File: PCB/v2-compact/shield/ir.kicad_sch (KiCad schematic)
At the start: 0 parts

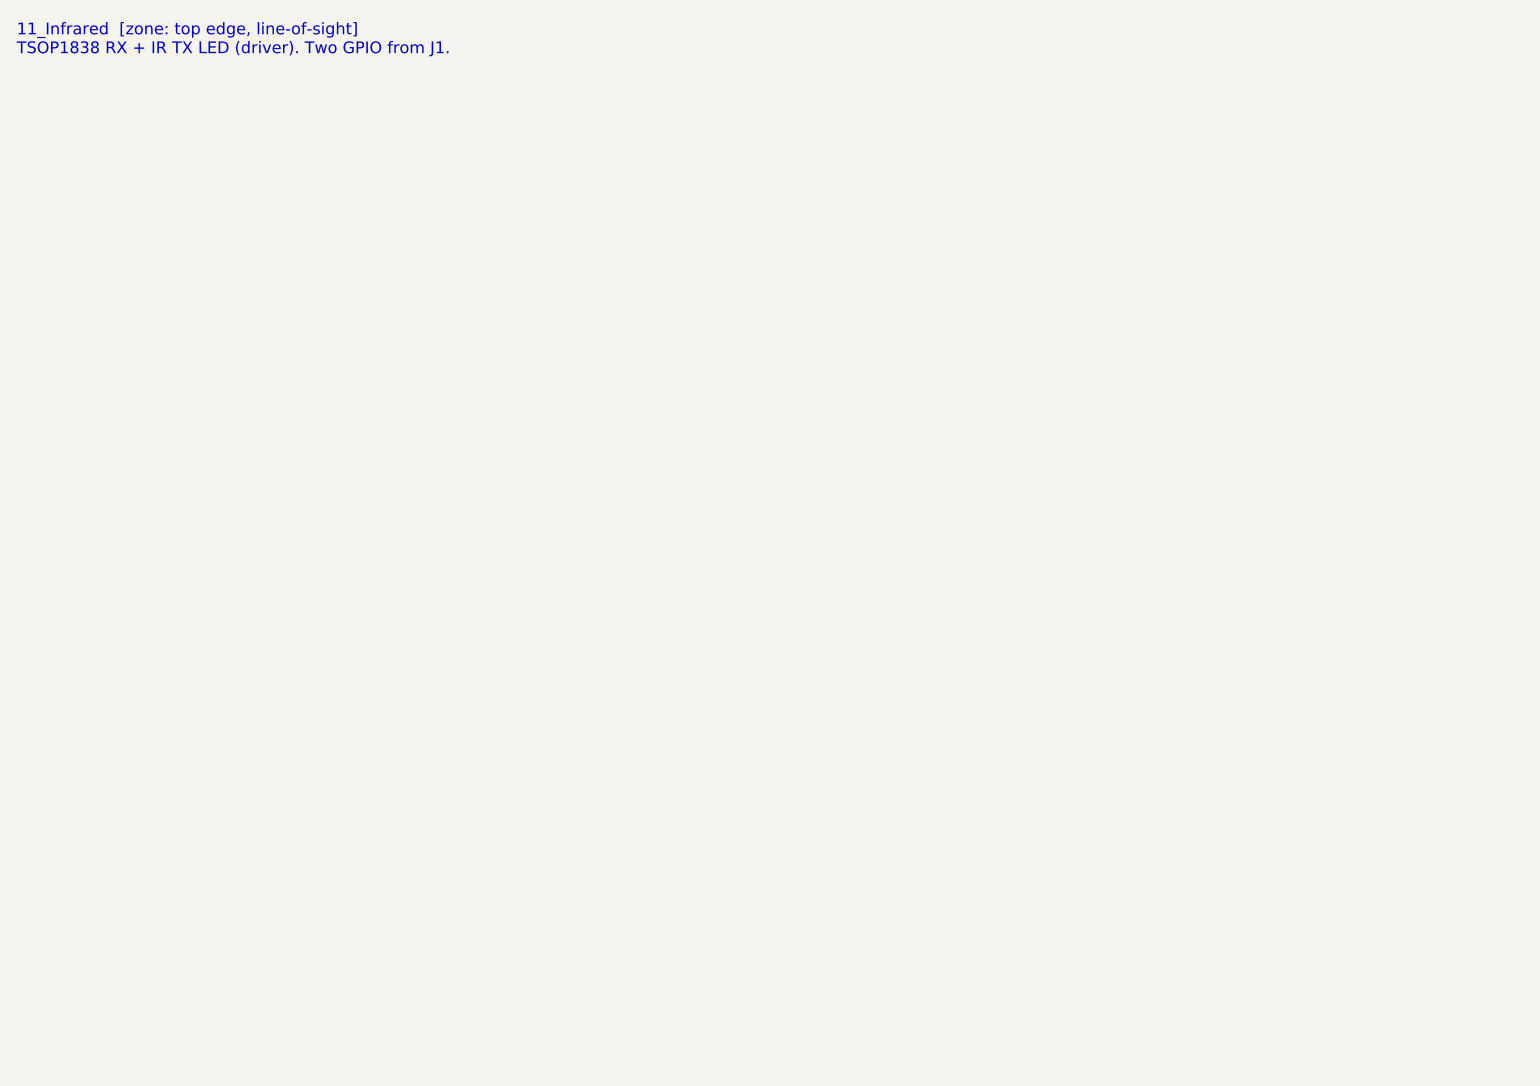
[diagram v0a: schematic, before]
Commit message: Schematics: capture PN532, GPS, IR, and both power sheets
- 07_NFC_PN532: I2C mode (I0/I1 set), 27.12MHz crystal, VMID cap, internal
  DVDD/SVDD regulator outputs correctly decoupled (not tied to 3V3), pull-ups;
  antenna pins flagged for the RF matching pass.
- 10_GPS: NEO-M9N UART to the C5, power + decoupling; bias-tee/antenna flagged.
- 11_IR: TSOP receiver + IR-LED transmitter (NPN driver).
- 02_Power (shield): local AP7361C LDO for the C5 rail + bulk caps + PWR_FLAGs.
- 01_Power_USB (main): USB-C, CC resistors, USBLC6 ESD, AP7361C 3V3 LDO.

All netlist-verified. Remaining ERC items are expected WIP (no-connects on unused
IC pins + power flags), to be cleaned once the MCU sheets tie in the shared nets.
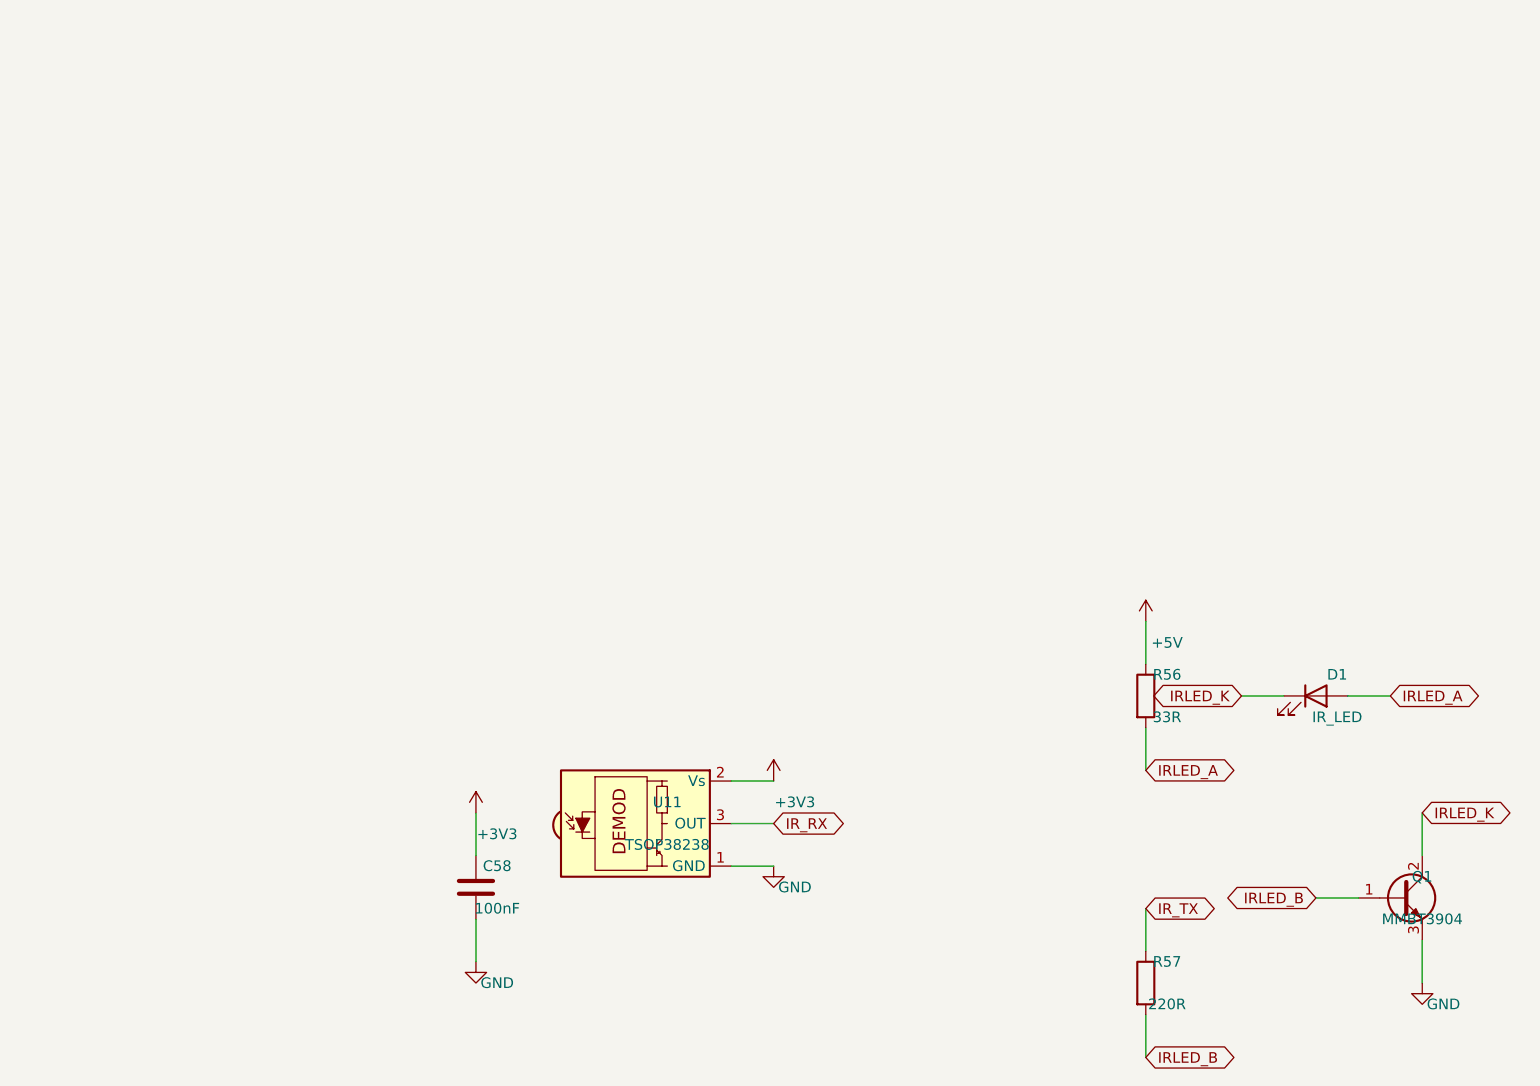
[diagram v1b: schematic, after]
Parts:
- added C58: 100nF, Capacitor_SMD:C_0402_1005Metric, symbol Device:C
- added D1: IR_LED, LED_SMD:LED_0805_2012Metric, symbol Device:LED
- added Q1: MMBT3904, Package_TO_SOT_SMD:SOT-23, symbol Transistor_BJT:Q_NPN_BCE
- added R56: 33R, Resistor_SMD:R_0402_1005Metric, symbol Device:R
- added R57: 220R, Resistor_SMD:R_0402_1005Metric, symbol Device:R
- added U11: TSOP38238, OptoDevice:Vishay_CAST-3Pin, symbol Interface_Optical:TSOP17xx
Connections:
- new net +3V3: C58.1, U11.2 (Vs)
- new net +5V: R56.1
- new net GND: C58.2, Q1.3 (E), U11.1 (GND)
- new net IRLED_A: D1.2 (A), R56.2
- new net IRLED_B: Q1.1 (B), R57.2
- new net IRLED_K: D1.1 (K), Q1.2 (C)
- new net IR_RX: U11.3 (OUT)
- new net IR_TX: R57.1
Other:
- note removed: "11_Infrared [zone: top edge, line-of-sight] TSOP1838 RX + IR TX LED (driver). Two GPIO from J1."
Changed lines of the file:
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@@
   (paper "A4")
   (title_block (title "11_IR") (company "YurilLAB"))
-  (text "11_Infrared  [zone: top edge, line-of-sight]
-TSOP1838 RX + IR TX LED (driver). Two GPIO from J1." (at 15 15 0)
-    (effects (font (size 1.4 1.4)) (justify left top)))
+  (symbol (lib_id "Interface_Optical:TSOP17xx") (at 90.17 110.49 0) (unit 1)
+    (in_bom yes) (on_board yes) (dnp no)
+    (property "Reference" "U11" (at 92.71 107.95 0) (effects (font (size 1.27 1.27))))
+    (property "Value" "TSOP38238" (at 92.71 113.03 0) (effects (font (size 1.27 1.27))))
+    (property "Footprint" "OptoDevice:Vishay_CAST-3Pin" (at 90.17 110.49 0) (effects (font (size 1.27 1.27)) hide))
+    (pin "1")
+    (pin "2")
+    (pin "3")
+    (instances (project "SnowOwl-Shield" (path "/76ddc4c2-3c0b-4070-9054-b9b062b12a9d" (reference "U11") (unit 1))))
+  )
+  (wire (pts (xy 100.33 115.57) (xy 105.41 115.57)) (stroke (width 0) (type default)))
+  (symbol (lib_id "power:GND") (at 105.41 115.57 0) (unit 1)
+    (in_bom yes) (on_board yes) (dnp no)
+    (property "Reference" "#PWR30F24C9" (at 107.95 113.03 0) (effects (font (size 1.27 1.27)) hide))
+    (property "Value" "GND" (at 107.95 118.11 0) (effects (font (size 1.27 1.27))))
+    (property "Footprint" "" (at 105.41 115.57 0) (effects (font (size 1.27 1.27)) hide))
+    (pin "1")
+    (instances (project "SnowOwl-Shield" (path "/76ddc4c2-3c0b-4070-9054-b9b062b12a9d" (reference "#PWR30F24C9") (unit 1))))
+  )
+  (wire (pts (xy 100.33 105.41) (xy 105.41 105.41)) (stroke (width 0) (type default)))
+  (symbol (lib_id "power:+3V3") (at 105.41 105.41 0) (unit 1)
+    (in_bom yes) (on_board yes) (dnp no)
+    (property "Reference" "#PWR271AF9C" (at 107.95 102.87 0) (effects (font (size 1.27 1.27)) hide))
+    (property "Value" "+3V3" (at 107.95 107.95 0) (effects (font (size 1.27 1.27))))
+    (property "Footprint" "" (at 105.41 105.41 0) (effects (font (size 1.27 1.27)) hide))
+    (pin "1")
+    (instances (project "SnowOwl-Shield" (path "/76ddc4c2-3c0b-4070-9054-b9b062b12a9d" (reference "#PWR271AF9C") (unit 1))))
+  )
+  (wire (pts (xy 100.33 110.49) (xy 105.41 110.49)) (stroke (width 0) (type default)))
+  (global_label "IR_RX" (shape bidirectional) (at 105.41 110.49 0) (fields_autoplaced)
+    (effects (font (size 1.27 1.27)) (justify left)))
+  (symbol (lib_id "Device:C") (at 69.85 118.11 0) (unit 1)
+    (in_bom yes) (on_board yes) (dnp no)
+    (property "Reference" "C58" (at 72.39 115.57 0) (effects (font (size 1.27 1.27))))
+    (property "Value" "100nF" (at 72.39 120.65 0) (effects (font (size 1.27 1.27))))
+    (property "Footprint" "Capacitor_SMD:C_0402_1005Metric" (at 69.85 118.11 0) (effects (font (size 1.27 1.27)) hide))
+    (pin "1")
+    (pin "2")
+    (instances (project "SnowOwl-Shield" (path "/76ddc4c2-3c0b-4070-9054-b9b062b12a9d" (reference "C58") (unit 1))))
+  )
+  (wire (pts (xy 69.85 114.3) (xy 69.85 109.22)) (stroke (width 0) (type default)))
+  (symbol (lib_id "power:+3V3") (at 69.85 109.22 0) (unit 1)
+    (in_bom yes) (on_board yes) (dnp no)
+    (property "Reference" "#PWR424FA62" (at 72.39 106.68 0) (effects (font (size 1.27 1.27)) hide))
+    (property "Value" "+3V3" (at 72.39 111.76 0) (effects (font (size 1.27 1.27))))
+    (property "Footprint" "" (at 69.85 109.22 0) (effects (font (size 1.27 1.27)) hide))
+    (pin "1")
+    (instances (project "SnowOwl-Shield" (path "/76ddc4c2-3c0b-4070-9054-b9b062b12a9d" (reference "#PWR424FA62") (unit 1))))
+  )
+  (wire (pts (xy 69.85 121.92) (xy 69.85 127)) (stroke (width 0) (type default)))
+  (symbol (lib_id "power:GND") (at 69.85 127 0) (unit 1)
+    (in_bom yes) (on_board yes) (dnp no)
+    (property "Reference" "#PWR752CC04" (at 72.39 124.46 0) (effects (font (size 1.27 1.27)) hide))
+    (property "Value" "GND" (at 72.39 129.54 0) (effects (font (size 1.27 1.27))))
+    (property "Footprint" "" (at 69.85 127 0) (effects (font (size 1.27 1.27)) hide))
+    (pin "1")
+    (instances (project "SnowOwl-Shield" (path "/76ddc4c2-3c0b-4070-9054-b9b062b12a9d" (reference "#PWR752CC04") (unit 1))))
+  )
+  (symbol (lib_id "Device:LED") (at 170.18 95.25 0) (unit 1)
+    (in_bom yes) (on_board yes) (dnp no)
+    (property "Reference" "D1" (at 172.72 92.71 0) (effects (font (size 1.27 1.27))))
+    (property "Value" "IR_LED" (at 172.72 97.79 0) (effects (font (size 1.27 1.27))))
+    (property "Footprint" "LED_SMD:LED_0805_2012Metric" (at 170.18 95.25 0) (effects (font (size 1.27 1.27)) hide))
+    (pin "1")
+    (pin "2")
+    (instances (project "SnowOwl-Shield" (path "/76ddc4c2-3c0b-4070-9054-b9b062b12a9d" (reference "D1") (unit 1))))
+  )
+  (wire (pts (xy 166.37 95.25) (xy 161.29 95.25)) (stroke (width 0) (type default)))
+  (global_label "IRLED_K" (shape bidirectional) (at 161.29 95.25 180) (fields_autoplaced)
+    (effects (font (size 1.27 1.27)) (justify right)))
+  (wire (pts (xy 173.99 95.25) (xy 179.07 95.25)) (stroke (width 0) (type default)))
+  (global_label "IRLED_A" (shape bidirectional) (at 179.07 95.25 0) (fields_autoplaced)
+    (effects (font (size 1.27 1.27)) (justify left)))
+  (symbol (lib_id "Device:R") (at 149.86 95.25 0) (unit 1)
+    (in_bom yes) (on_board yes) (dnp no)
+    (property "Reference" "R56" (at 152.4 92.71 0) (effects (font (size 1.27 1.27))))
+    (property "Value" "33R" (at 152.4 97.79 0) (effects (font (size 1.27 1.27))))
+    (property "Footprint" "Resistor_SMD:R_0402_1005Metric" (at 149.86 95.25 0) (effects (font (size 1.27 1.27)) hide))
+    (pin "1")
+    (pin "2")
+    (instances (project "SnowOwl-Shield" (path "/76ddc4c2-3c0b-4070-9054-b9b062b12a9d" (reference "R56") (unit 1))))
+  )
+  (wire (pts (xy 149.86 91.44) (xy 149.86 86.36)) (stroke (width 0) (type default)))
+  (symbol (lib_id "power:+5V") (at 149.86 86.36 0) (unit 1)
+    (in_bom yes) (on_board yes) (dnp no)
+    (property "Reference" "#PWR7F595ED" (at 152.4 83.82 0) (effects (font (size 1.27 1.27)) hide))
+    (property "Value" "+5V" (at 152.4 88.9 0) (effects (font (size 1.27 1.27))))
+    (property "Footprint" "" (at 149.86 86.36 0) (effects (font (size 1.27 1.27)) hide))
+    (pin "1")
+    (instances (project "SnowOwl-Shield" (path "/76ddc4c2-3c0b-4070-9054-b9b062b12a9d" (reference "#PWR7F595ED") (unit 1))))
+  )
+  (wire (pts (xy 149.86 99.06) (xy 149.86 104.14)) (stroke (width 0) (type default)))
+  (global_label "IRLED_A" (shape bidirectional) (at 149.86 104.14 0) (fields_autoplaced)
+    (effects (font (size 1.27 1.27)) (justify left)))
+  (symbol (lib_id "Transistor_BJT:Q_NPN_BCE") (at 180.34 119.38 0) (unit 1)
+    (in_bom yes) (on_board yes) (dnp no)
+    (property "Reference" "Q1" (at 182.88 116.84 0) (effects (font (size 1.27 1.27))))
+    (property "Value" "MMBT3904" (at 182.88 121.92 0) (effects (font (size 1.27 1.27))))
+    (property "Footprint" "Package_TO_SOT_SMD:SOT-23" (at 180.34 119.38 0) (effects (font (size 1.27 1.27)) hide))
+    (pin "1")
+    (pin "2")
+    (pin "3")
+    (instances (project "SnowOwl-Shield" (path "/76ddc4c2-3c0b-4070-9054-b9b062b12a9d" (reference "Q1") (unit 1))))
+  )
+  (wire (pts (xy 175.26 119.38) (xy 170.18 119.38)) (stroke (width 0) (type default)))
+  (global_label "IRLED_B" (shape bidirectional) (at 170.18 119.38 180) (fields_autoplaced)
+    (effects (font (size 1.27 1.27)) (justify right)))
+  (wire (pts (xy 182.88 114.3) (xy 182.88 109.22)) (stroke (width 0) (type default)))
+  (global_label "IRLED_K" (shape bidirectional) (at 182.88 109.22 0) (fields_autoplaced)
+    (effects (font (size 1.27 1.27)) (justify left)))
+  (wire (pts (xy 182.88 124.46) (xy 182.88 129.54)) (stroke (width 0) (type default)))
+  (symbol (lib_id "power:GND") (at 182.88 129.54 0) (unit 1)
+    (in_bom yes) (on_board yes) (dnp no)
+    (property "Reference" "#PWRAD293A0" (at 185.42 127 0) (effects (font (size 1.27 1.27)) hide))
+    (property "Value" "GND" (at 185.42 132.08 0) (effects (font (size 1.27 1.27))))
+    (property "Footprint" "" (at 182.88 129.54 0) (effects (font (size 1.27 1.27)) hide))
+    (pin "1")
+    (instances (project "SnowOwl-Shield" (path "/76ddc4c2-3c0b-4070-9054-b9b062b12a9d" (reference "#PWRAD293A0") (unit 1))))
+  )
+  (symbol (lib_id "Device:R") (at 149.86 129.54 0) (unit 1)
+    (in_bom yes) (on_board yes) (dnp no)
+    (property "Reference" "R57" (at 152.4 127 0) (effects (font (size 1.27 1.27))))
+    (property "Value" "220R" (at 152.4 132.08 0) (effects (font (size 1.27 1.27))))
+    (property "Footprint" "Resistor_SMD:R_0402_1005Metric" (at 149.86 129.54 0) (effects (font (size 1.27 1.27)) hide))
+    (pin "1")
+    (pin "2")
+    (instances (project "SnowOwl-Shield" (path "/76ddc4c2-3c0b-4070-9054-b9b062b12a9d" (reference "R57") (unit 1))))
+  )
+  (wire (pts (xy 149.86 125.73) (xy 149.86 120.65)) (stroke (width 0) (type default)))
+  (global_label "IR_TX" (shape bidirectional) (at 149.86 120.65 0) (fields_autoplaced)
+    (effects (font (size 1.27 1.27)) (justify left)))
+  (wire (pts (xy 149.86 133.35) (xy 149.86 138.43)) (stroke (width 0) (type default)))
+  (global_label "IRLED_B" (shape bidirectional) (at 149.86 138.43 0) (fields_autoplaced)
+    (effects (font (size 1.27 1.27)) (justify left)))
   (sheet_instances (path "/" (page "1")))
 )
